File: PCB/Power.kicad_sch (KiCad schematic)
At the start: 14 parts, among them J10 USB_C_Receptacle_USB2.0_14P, U1 TLV62569ADRL, U4 CP2102N-Axx-xQFN28

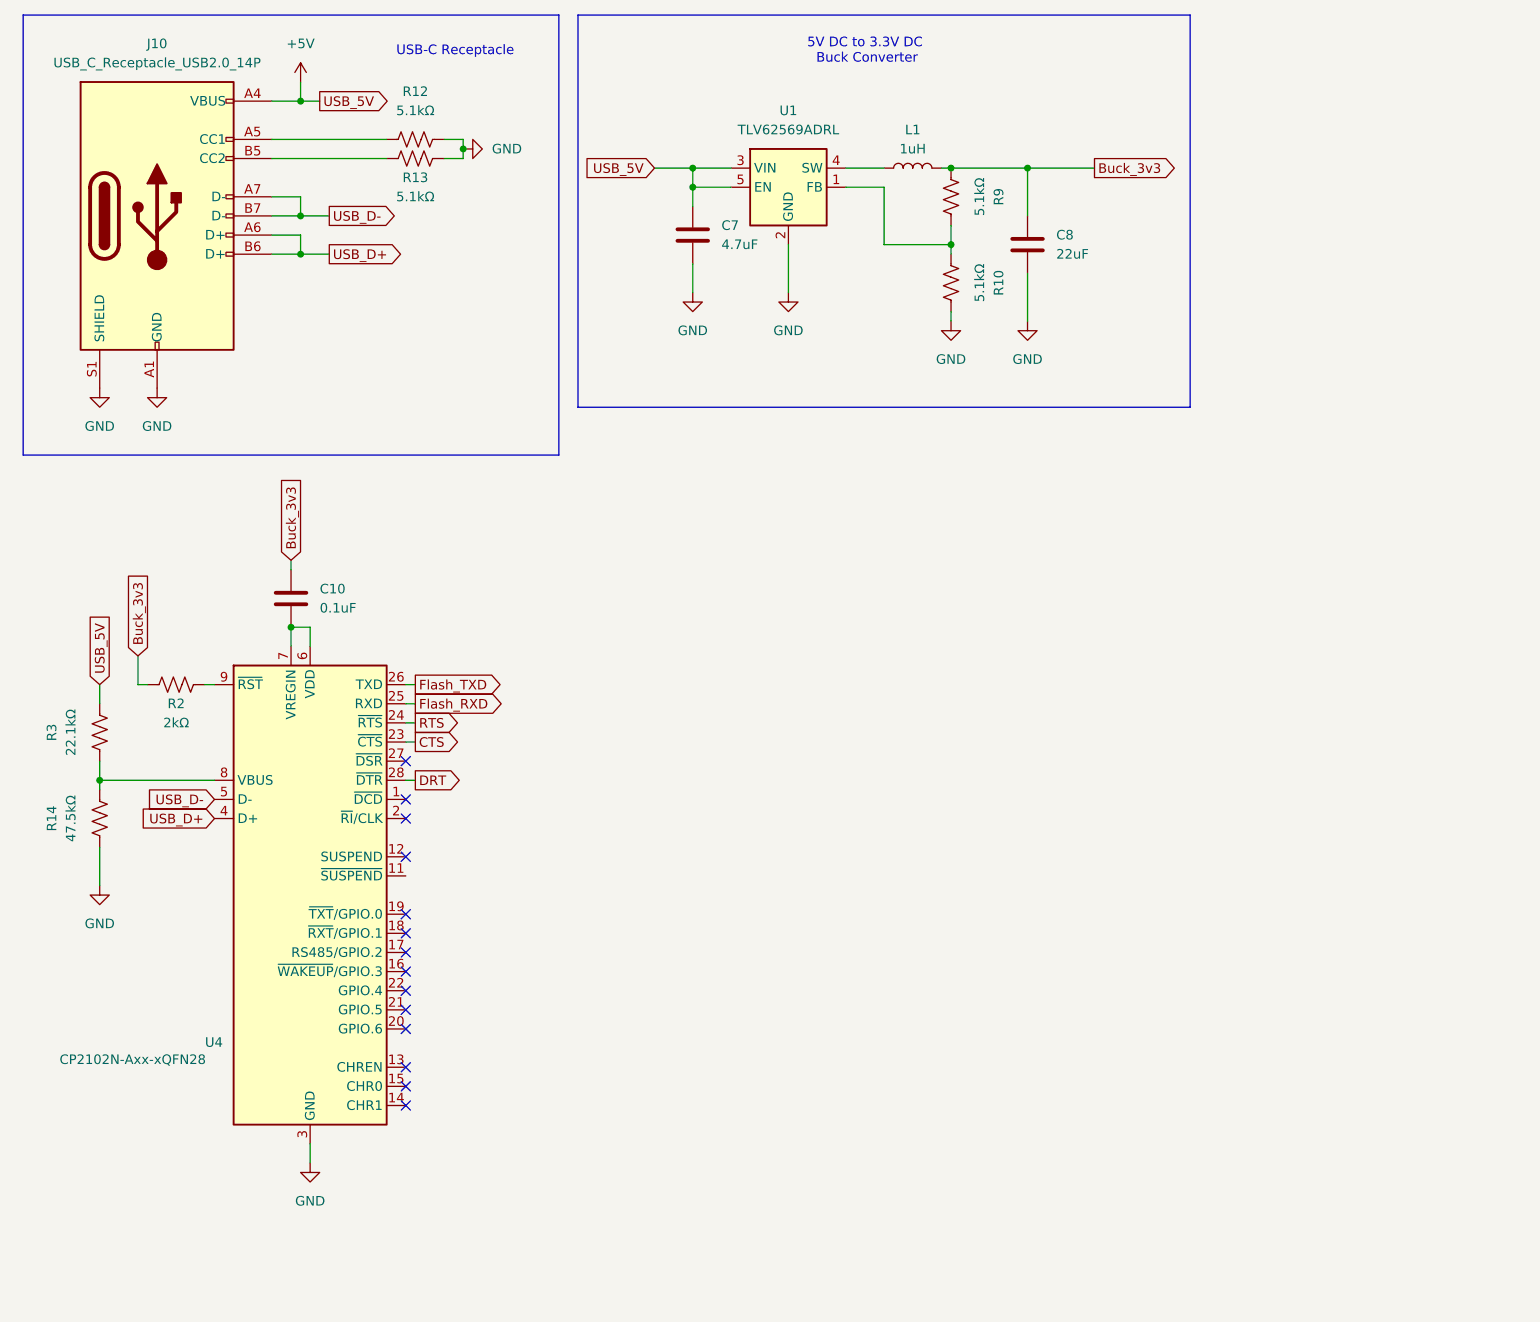
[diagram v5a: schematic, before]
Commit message: Added IO0 button
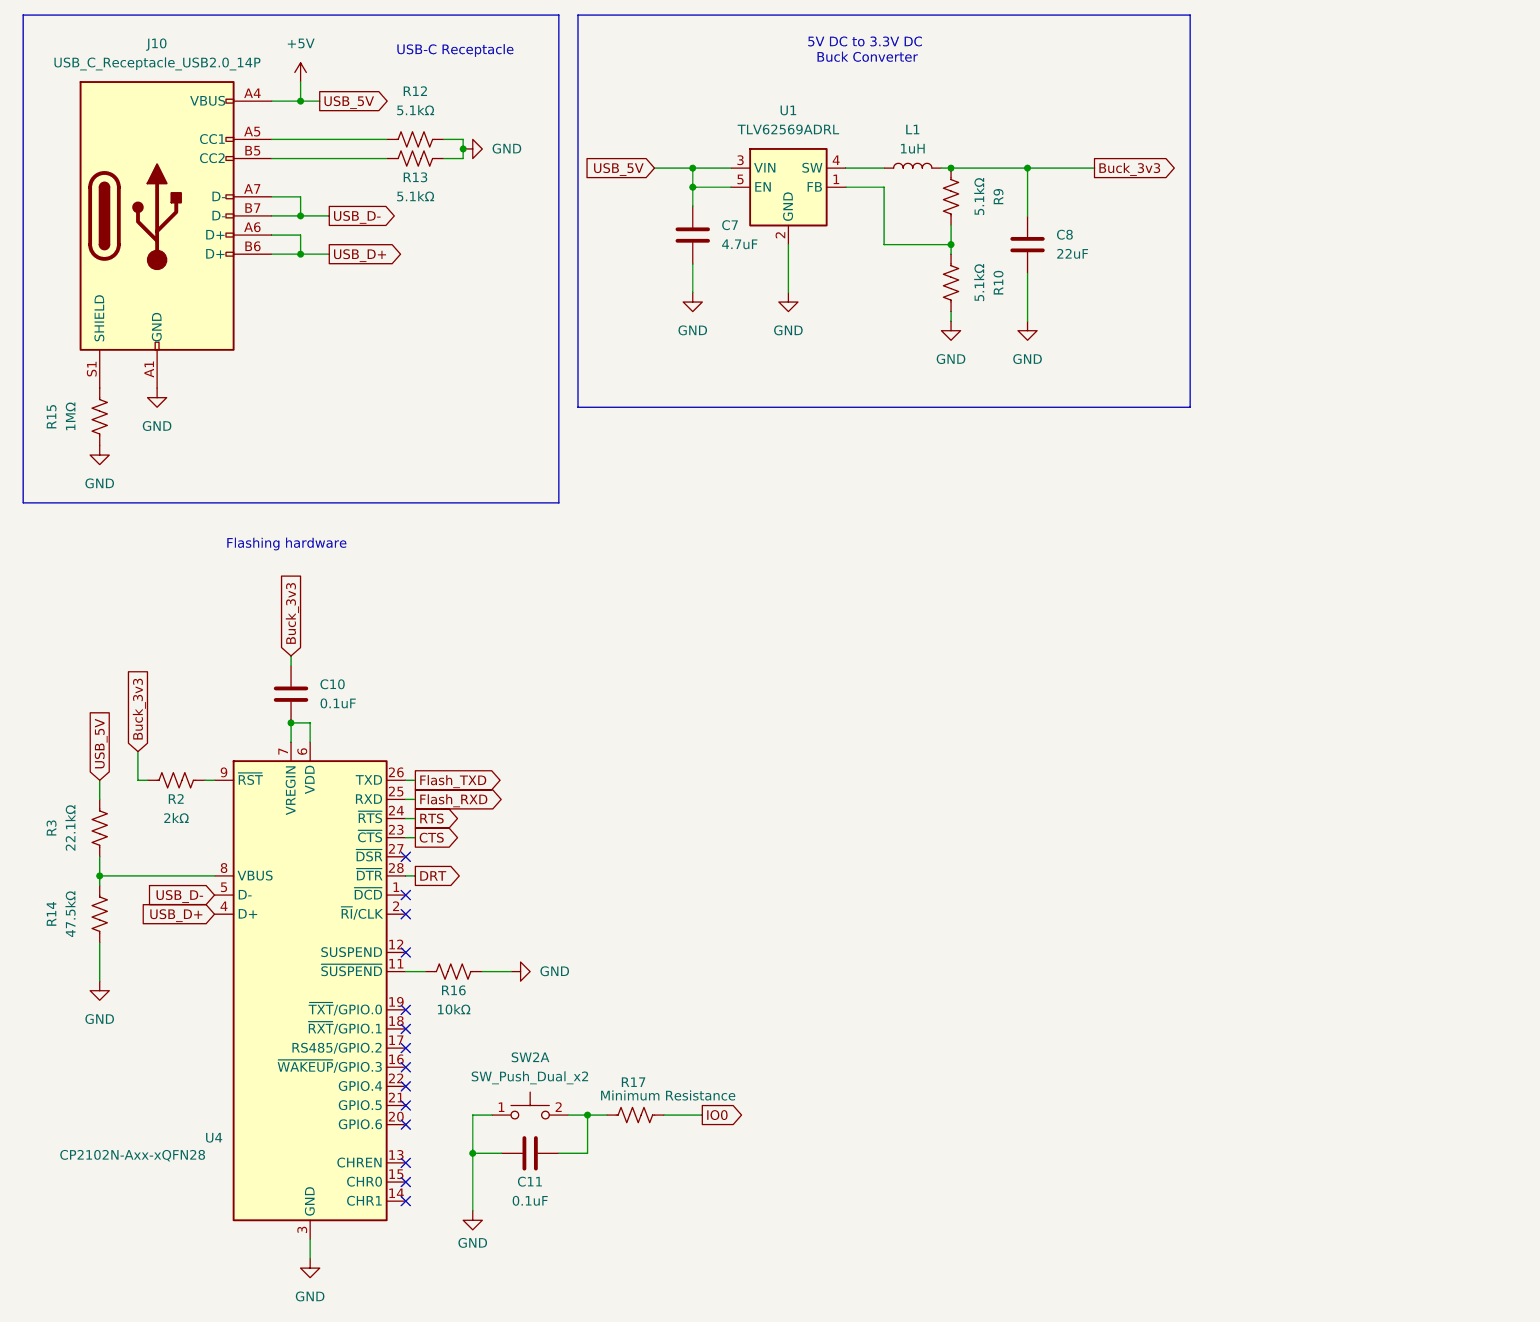
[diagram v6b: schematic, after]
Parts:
- added C11: 0.1uF, Capacitor_SMD:C_1206_3216Metric_Pad1.33x1.80mm_HandSolder, symbol Device:C
- added R15: 1MΩ, Resistor_SMD:R_1206_3216Metric_Pad1.30x1.75mm_HandSolder, symbol Device:R_US
- added R16: 10kΩ, Resistor_SMD:R_1206_3216Metric_Pad1.30x1.75mm_HandSolder, symbol Device:R_US
- added R17: Minimum Resistance, Resistor_SMD:R_1206_3216Metric_Pad1.30x1.75mm_HandSolder, symbol Device:R_US
- added SW2: SW_Push_Dual_x2, SMD_Button:Shop_SMD_Button, symbol Switch:SW_Push_Dual_x2
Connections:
- net GND: now also C11.2, R15.1, R16.2, SW2.1 (C); no longer J10.S1 (SHIELD)
- net at U4.11 (~{SUSPEND}): now also R16.1
- new net: C11.1, R17.1, SW2.2 (D)
- new net: J10.S1 (SHIELD), R15.2
- new net IO0: R17.2
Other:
- note added: "Flashing hardware"
- moved on the sheet: C10, R14, R2, R3, U4

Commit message: add power indicator LEDs, connect peripherals
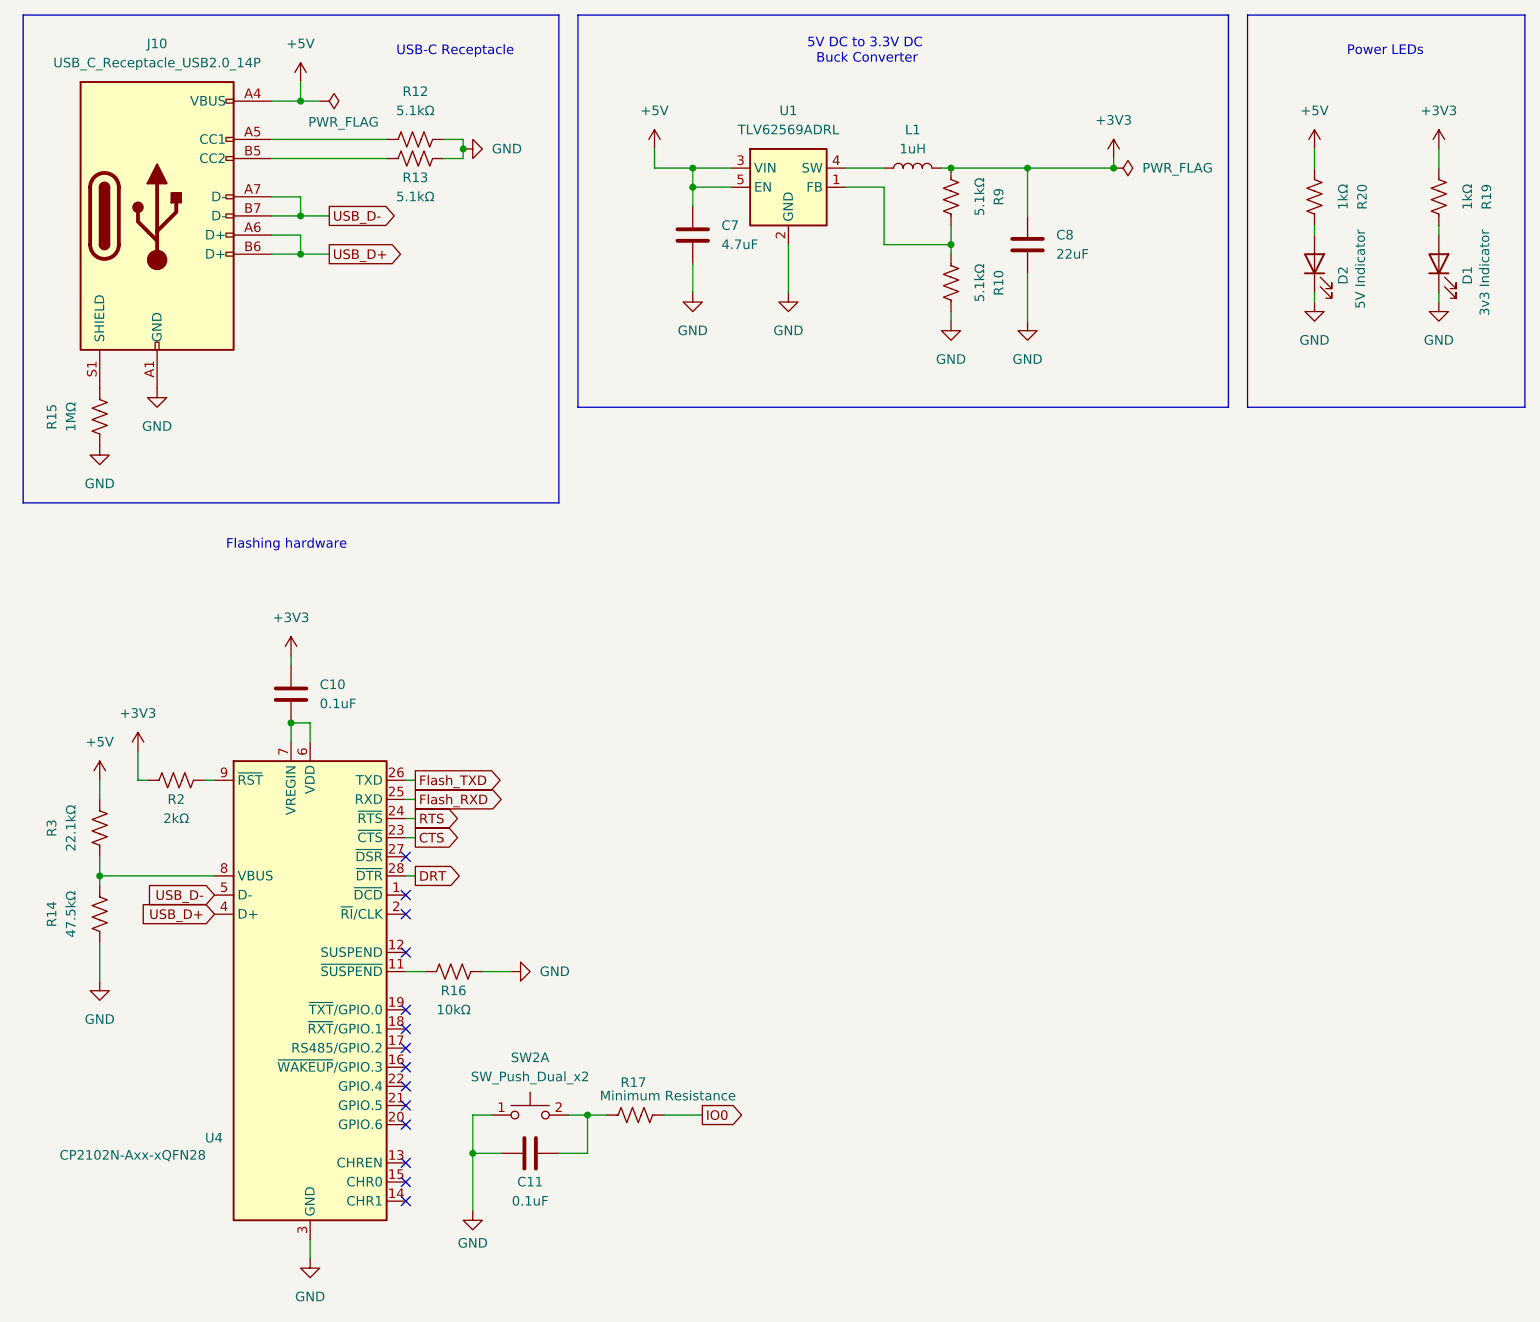
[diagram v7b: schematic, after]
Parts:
- added D1: 3v3 Indicator, symbol Device:LED
- added D2: 5V Indicator, symbol Device:LED
- added R19, R20: 1kΩ, Resistor_SMD:R_1206_3216Metric_Pad1.30x1.75mm_HandSolder, symbol Device:R_US
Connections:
- net +5V: now also R20.1
- net GND: now also D1.1 (K), D2.1 (K)
- net Buck_3v3 renamed +3V3
- net +3V3: now also R19.1
- new net: D1.2 (A), R19.2
- new net: D2.2 (A), R20.2
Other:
- note added: "Power LEDs"

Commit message: lots of 'final' schematic updates. ERC is essentially clean, PCB design can begin
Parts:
- removed SW2: SW_Push_Dual_x2, SMD_Button:Shop_SMD_Button, symbol Switch:SW_Push_Dual_x2
- added SW2: SW_Push, SMD_Button:Shop_SMD_Button, symbol Switch:SW_Push
- D1, D2: footprint (none) -> LED_SMD:LED_0603_1608Metric_Pad1.05x0.95mm_HandSolder
- R19: value 1kΩ -> 150Ω
- R20: value 1kΩ -> 330Ω
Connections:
- net GND: now also SW2.1
- net at C11.1, R17.1: now also SW2.2
